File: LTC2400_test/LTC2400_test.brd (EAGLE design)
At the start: 25.4 x 33 mm, 8 parts, among them U1 LTC2400CS8PBF

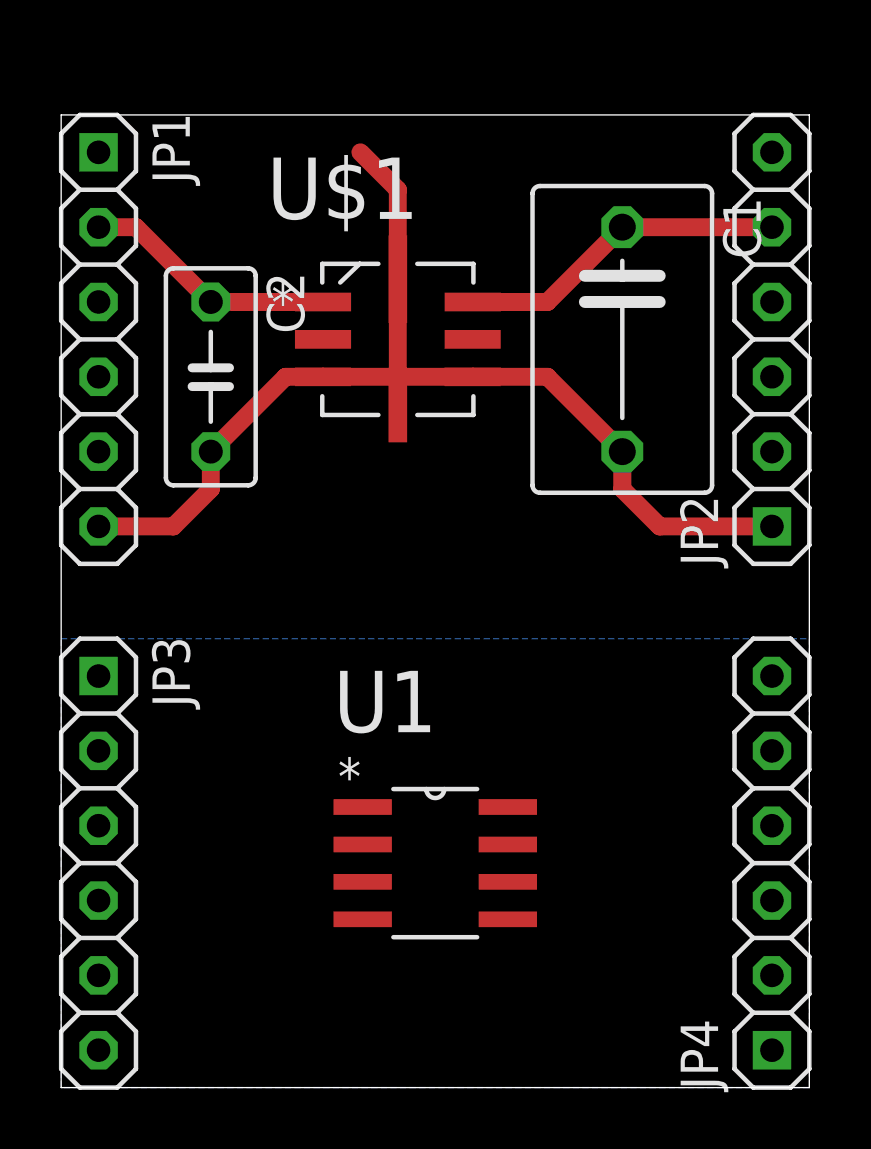
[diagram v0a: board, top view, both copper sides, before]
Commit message: * updated PB1 board, need a lot more lessons learned with it, so lets leave it for now * updated LTC2400 test board, going to focus on that first
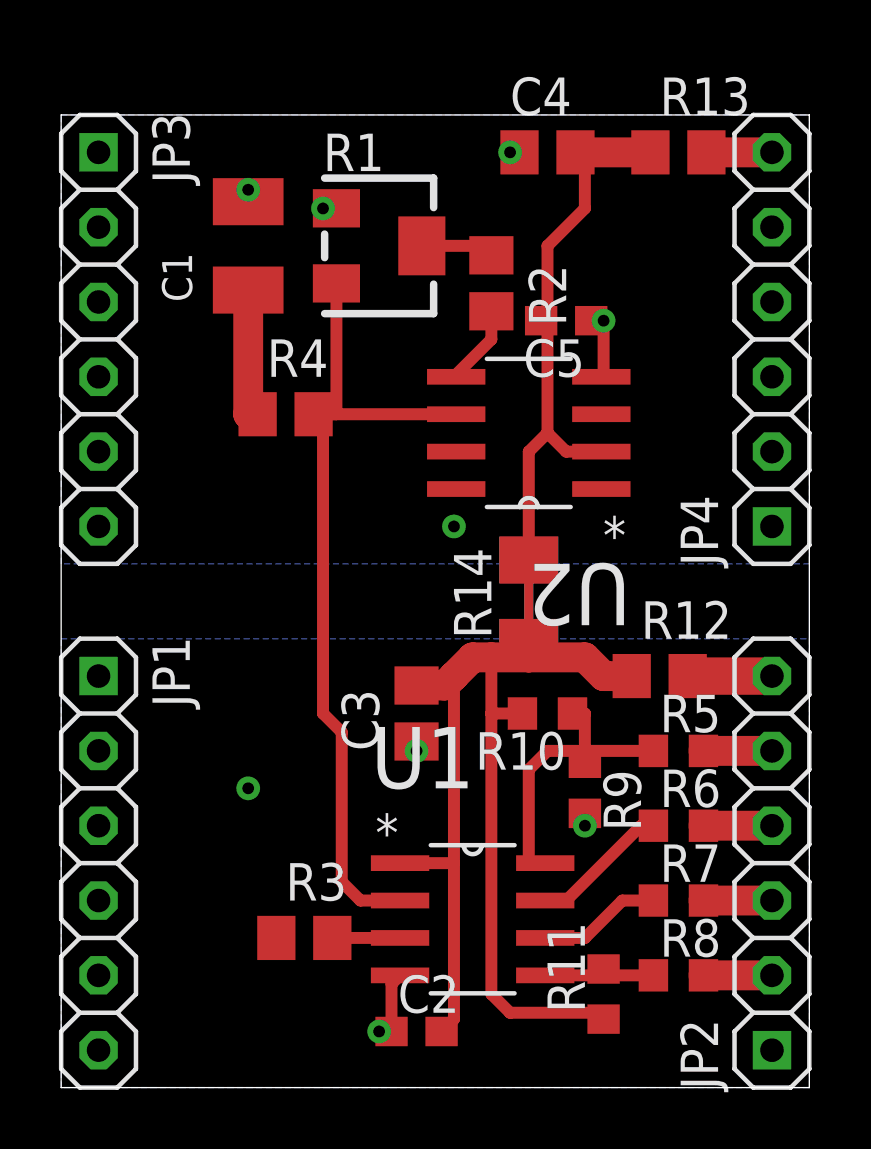
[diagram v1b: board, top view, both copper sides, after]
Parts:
- removed U$1: LTC6655LS8_ELONG, SquantorLinearTechnology:LS8_ELONG
- added C3, C4: 10u, SquantorRCL:C0805
- added C5: 100n, SquantorRCL:C0603
- added R1: 100k, SquantorRCL:RTRIM3214W
- added R10: 50Hz, SquantorRCL:R0603
- added R11: 10k, SquantorRCL:R0603
- added R12, R13: ferrite, SquantorRCL:R0805
- added R14, R15: (no value), SquantorRCL:M1206
- added R2: 4.7M, SquantorRCL:R0805
- added R3: 5.1k, SquantorRCL:R0805
- added R4: 2.2, SquantorRCL:R0805
- added R5, R6, R7, R8: 100, SquantorRCL:R0603
- added R9: 60Hz, SquantorRCL:R0603
- added U2: LT1019A-2.5PBFS8, SquantorLinearTechnology:SOIC127P600X175-8N
- C1: device SquantorRCL:C075-063X106 -> SquantorRCL:SMC_B
- C2: value (none) -> 100n; device SquantorRCL:C050-030X075 -> SquantorRCL:C0603
- U1: device SquantorLinearTechnology:SOIC127P600X175-8N -> SquantorLinearTechnology:SOIC127P600X175-8N@1
- moved C2 23.3 mm to (12.1, 1.91), turned to 0 degrees
- moved JP1 17.8 mm to (1.27, 7.62)
- moved JP2 17.8 mm to (24.1, 7.62)
- moved JP3 17.8 mm to (1.27, 25.4)
- moved JP4 17.8 mm to (24.1, 25.4)
- moved C1 13.1 mm to (6.35, 28.6), turned to 90 degrees
- moved U1 2.29 mm to (14.0, 5.71)
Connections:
- removed net VCC: U1.1
- new net +5V: C2.2, C3.2, C4.2, C5.2, R10.2, R11.1, R12.1, R13.1, R14.1, R14.2, U1.1, U2.2
- new net CS: R11.2, R8.1, U1.5
- new net FO: R10.1, R5.1, R9.1, U1.8
- new net N$1: JP4.6, R13.2
- new net N$10: R1.2, R2.1
- new net N$11: JP2.2, R8.2
- new net N$12: JP2.3, R7.2
- new net N$13: JP2.4, R6.2
- new net N$14: JP2.5, R5.2
- new net N$3: JP2.6, R12.2
- new net N$6: R3.2, U1.3
- new net REF_TEMP: U2.3
- new net SCK: R6.1, U1.7
- new net SDO: R7.1, U1.6
- new net TRIM: R2.2, U2.5
- new net VREF: R1.3, R4.2, U1.2, U2.6
- net GND: now also C1.-, C2.1, C3.1, C4.1, C5.1, JP1.2, JP1.4, R1.1, R15.1, R15.2, R9.2, U1.4, U2.4; no longer C1.2, C2.2, JP3.1, JP4.6, U$1.3, U$1.4, U$1.5, U$1.8
- net N$2: now also JP3.5; no longer C1.1, JP2.5, U$1.6, U$1.7
- net N$4: now also C1.+, R4.1; no longer C2.1, JP1.2, U$1.1, U$1.2
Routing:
- net +5V: track 0.00 -> 61.6 mm
- net GND: track 38.0 -> 9.20 mm, vias 0 -> 9
- net VREF: track 0.00 -> 28.6 mm
- net N$2: track 11.2 -> 0.00 mm
- net FO: track 0.00 -> 10.3 mm
- net SCK: track 0.00 -> 4.72 mm
- net SDO: track 0.00 -> 4.20 mm
- net N$4: track 8.67 -> 4.54 mm
- net CS: track 0.00 -> 3.89 mm
- net N$3: track 0.00 -> 2.86 mm
- net TRIM: track 0.00 -> 2.72 mm
- net N$10: track 0.00 -> 2.68 mm
- net N$14: track 0.00 -> 2.32 mm
- net N$13: track 0.00 -> 2.32 mm
- net N$12: track 0.00 -> 2.32 mm
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- added copper zone on layer 16, net GND
- removed copper zone on layer 16, net N$1
